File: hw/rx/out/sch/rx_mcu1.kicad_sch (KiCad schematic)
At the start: 21 parts, among them J2 SWD, U1 BT40E

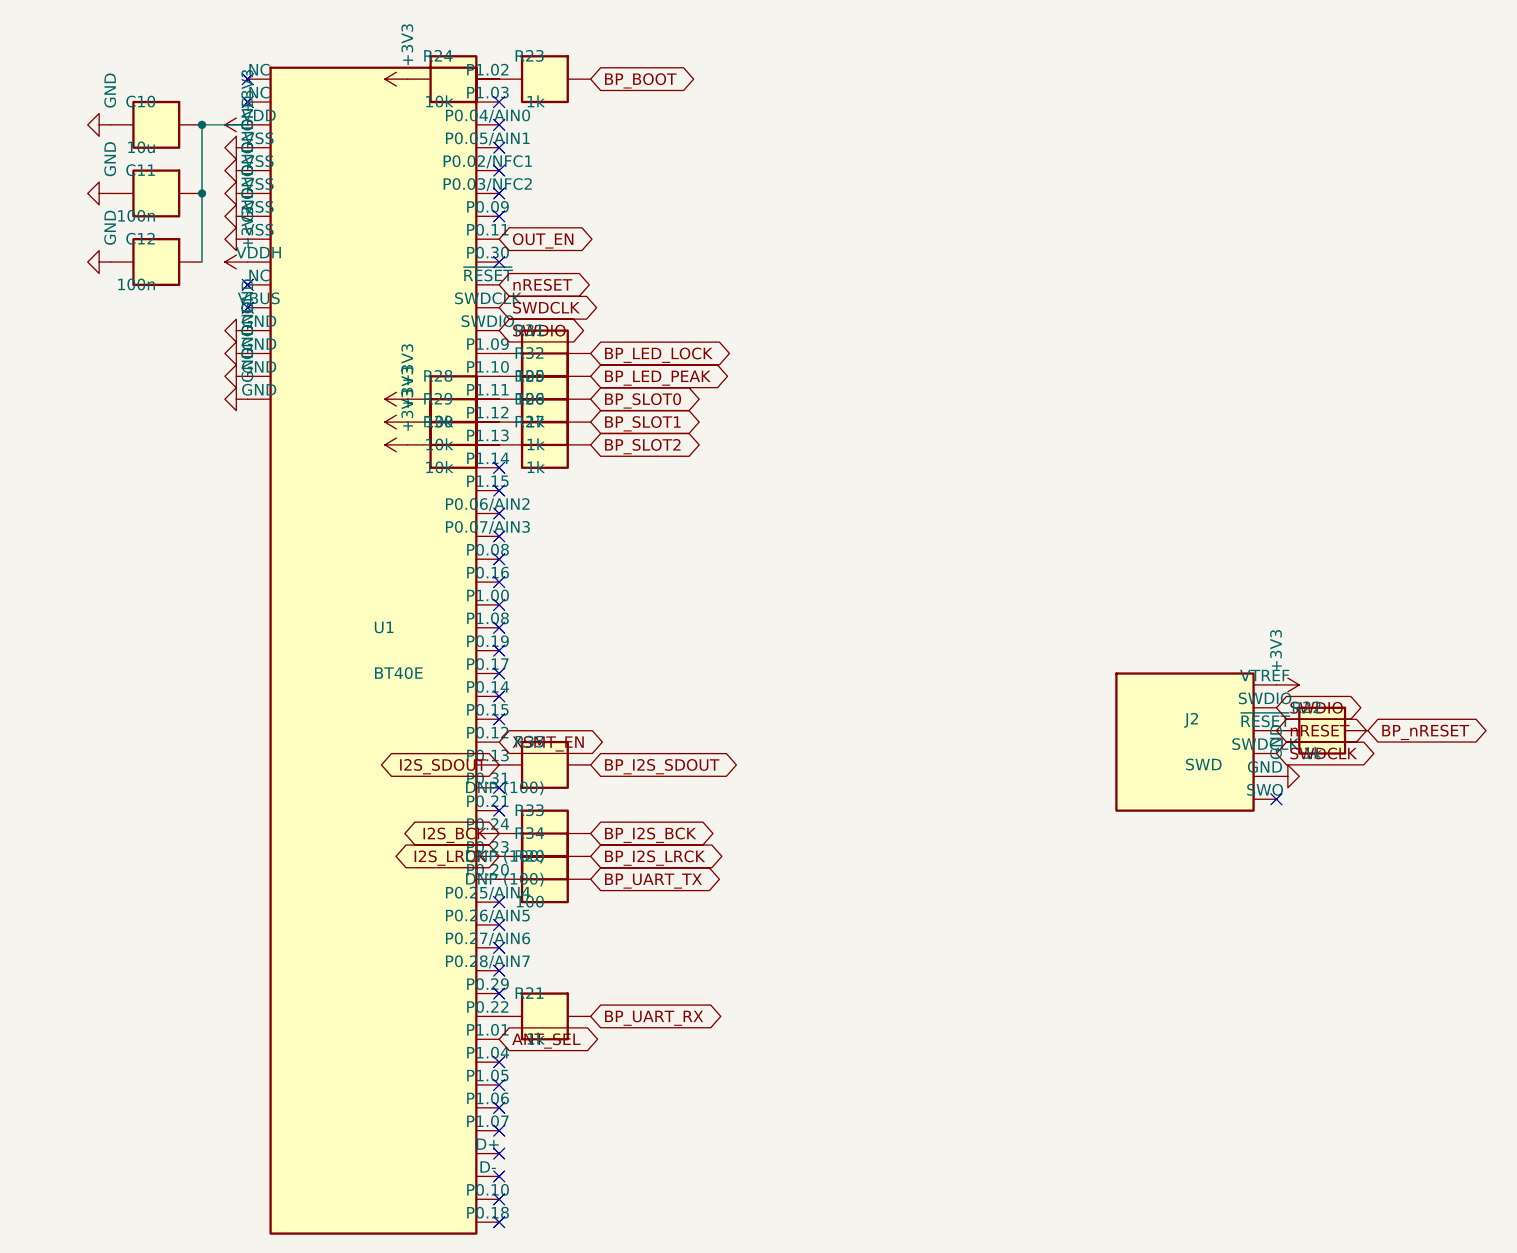
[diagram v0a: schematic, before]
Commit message: hw/rx + hw/pack: #116 review fixes: netclass pour clearances (no 0.09 mm override), keyed J1 with no hole at 14, solid RF grounds, K1 pin-1/CPL rotation, raw RF numbers (#34)
- M1: JLC copper-clearance rule removed from rx and pack .kicad_dru; boards refilled/regenerated; probe-rule tests
  assert >= 0.125 mm everywhere and >= 0.15 mm to Audio_I on the committed fill; outer-copper rule width-independent
- S1: openpack:PinHeader_2x13_P2.54mm_Key14 (pad 14 deleted, KEY silk), header XFCN PZ254V-12-26P (LCSC C22465887,
  pin 14 cut), main-board socket Samtec SSW-113-01-G-D-14 recorded in ADR-0014; test
- S2: zone_connect solid on J3-J5, U2, U1 GND pads; test
- S3: TQ2SA pin-1 dot + '+', CPL +270 for the relay (K1 at 180); pin-1 marker + CPL test for all polarized parts
- N1 raw RF Z0 (51.5 bare / ~49.3 masked), N3 C44 at U6, REVIEW follow-ups

Co-Authored-By: Claude Opus 5.5 <noreply@anthropic.com>
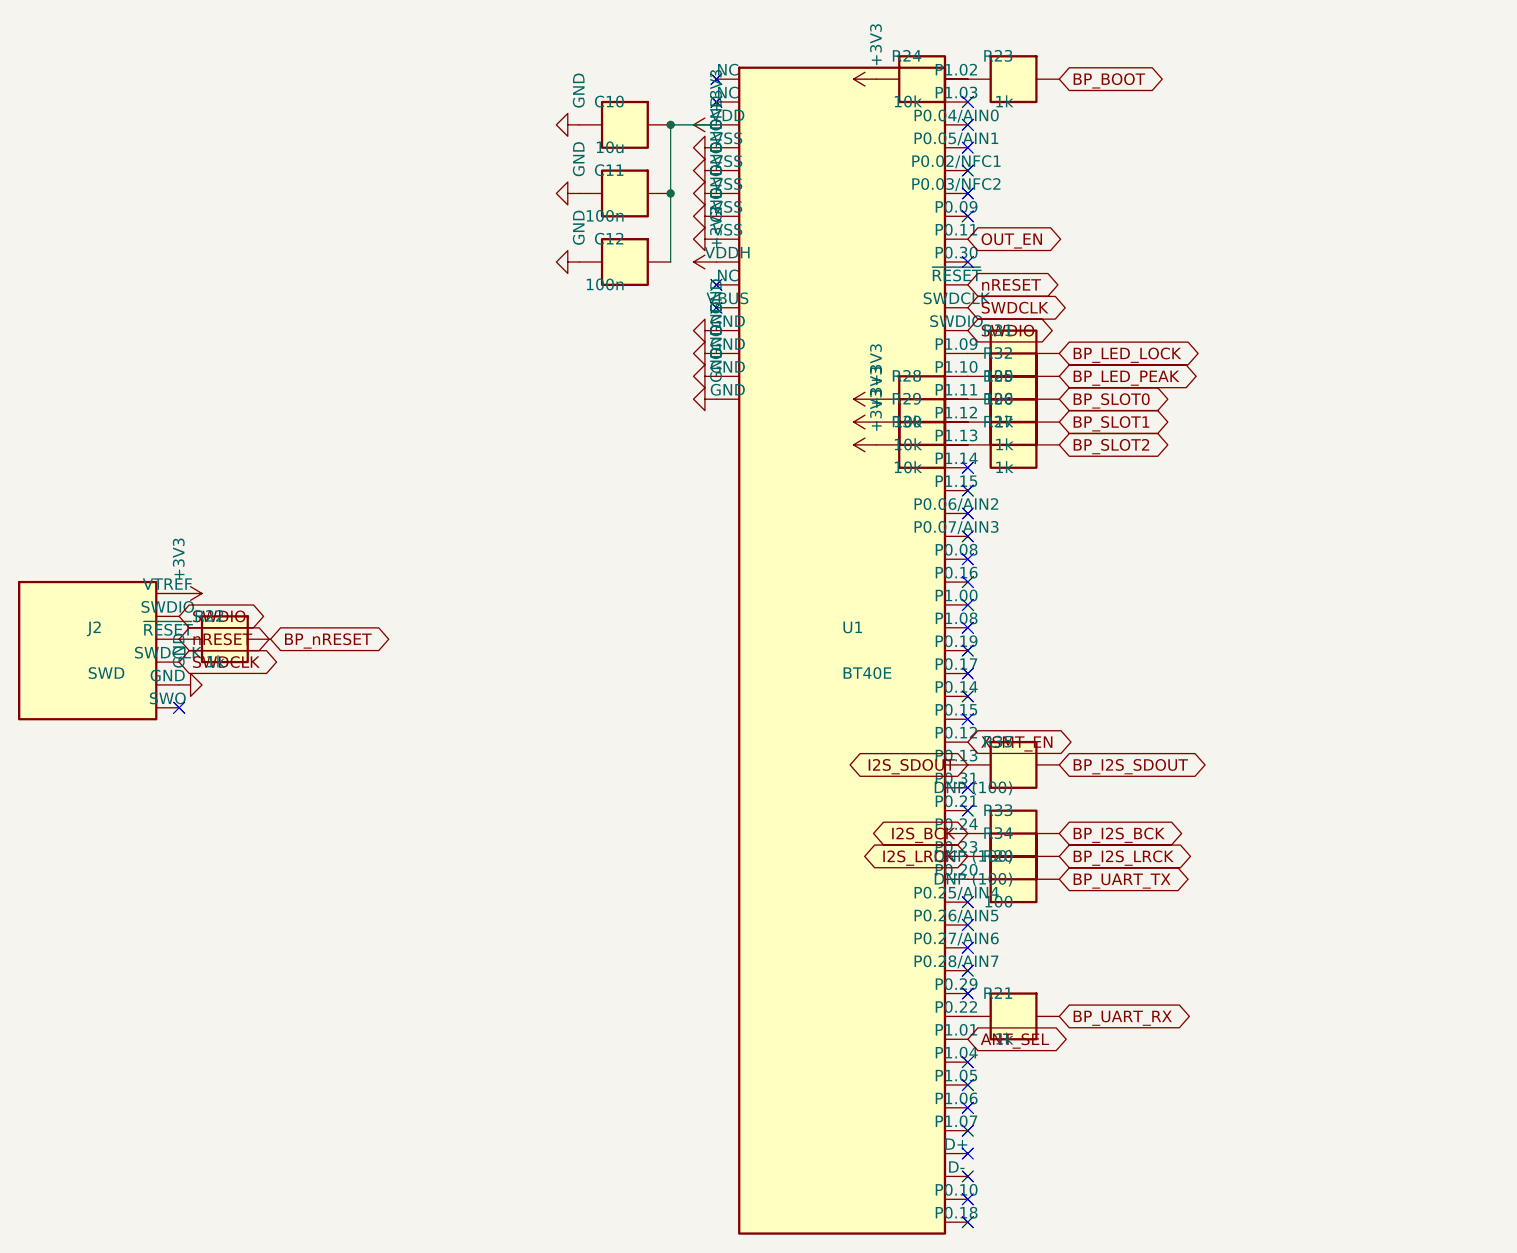
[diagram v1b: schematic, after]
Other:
- moved on the sheet: C10, C11, C12, J2, R20, R21, R22, R23, R24, R25, R26, R27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
